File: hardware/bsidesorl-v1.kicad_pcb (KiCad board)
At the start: 2 copper layers, 92 x 63.4 mm, 40 parts, among them J1 SAO Connector, Q1 SI2302S, SW1 MST22D18G2_125, U1 CH32V003F4P6, U2 TPS61021ADSGR

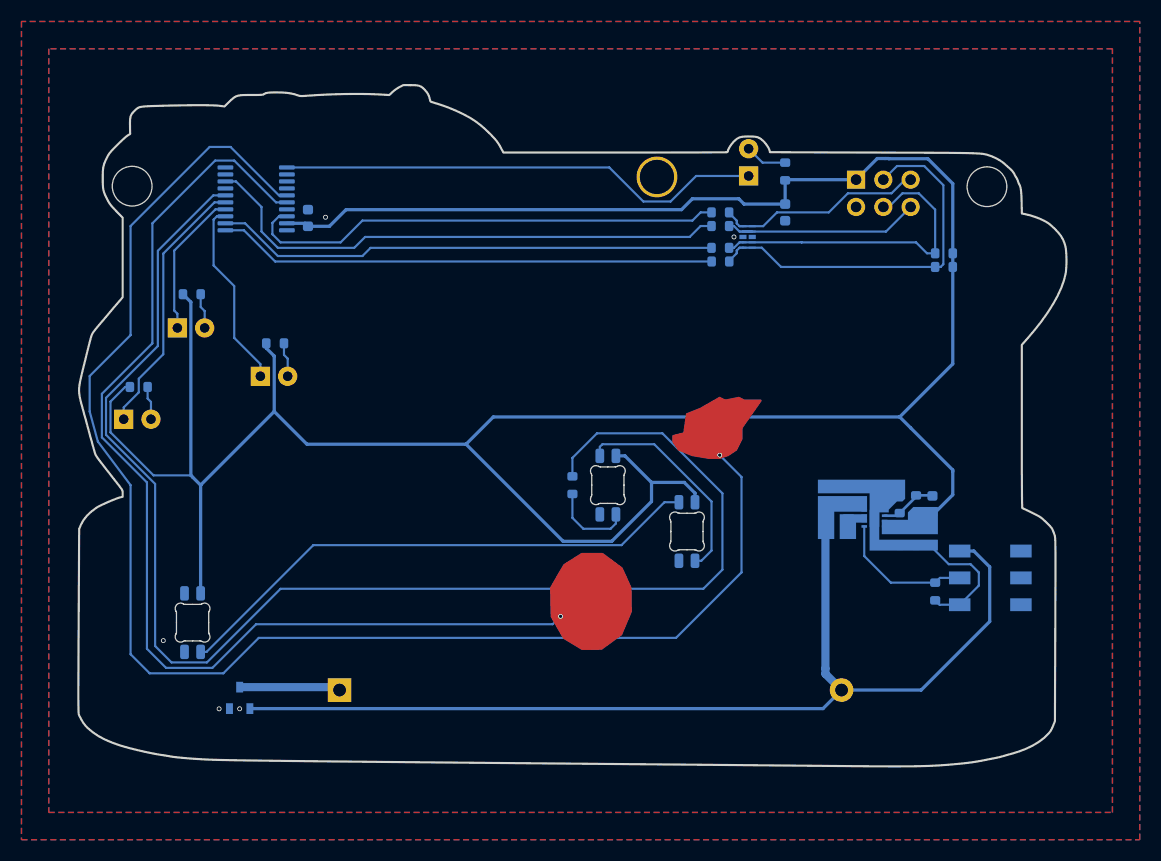
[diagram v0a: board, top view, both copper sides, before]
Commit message: Production PCB as ordered
* Fingerprint soldermask artwork and board outline sources
* SW1 excluded from BOM/CPL (hand-placed)
* Regenerated JLCPCB gerbers and production files
* Add mk_easyeda.py for importing the KiCad board into EasyEDA Pro
* Ignore local fab/order artifacts

Co-Authored-By: Claude Opus 5.5 (1M context) <noreply@anthropic.com>
Claude-Session: https://claude.ai/code/session_01VwuCpwoY4XUvmQLYcHynUX
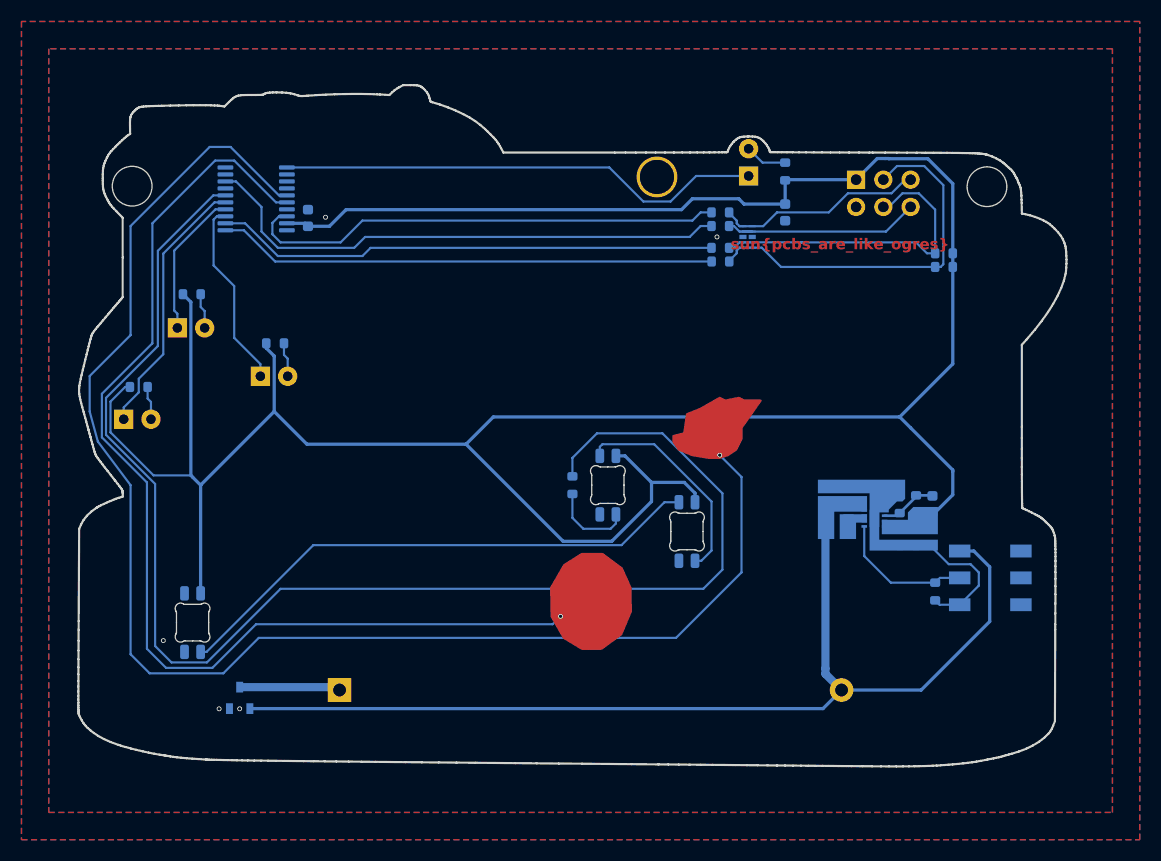
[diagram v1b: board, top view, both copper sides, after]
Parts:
- removed the G*** at (144.5, 99.0)
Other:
- outline, holes or cut-outs redrawn
- board text added: "LEDs and SAO connector go on the front. Battery holder and power switch go on the back (this side)."
- board text added: "sun{pcbs_are_like_ogres}"
